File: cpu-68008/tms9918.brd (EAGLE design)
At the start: 99.7 x 99.7 mm, 38 parts, among them IC1 74HCT574N, IC101 GAL22V10D, IC2 74HCT574N, IC3 74HCT574N, IC4 74HCT04N, IC5 AS6C62256, IC6 74HCT373N, IC7 TMS9918, Q401 10.73866 MHz, T1 2N3904

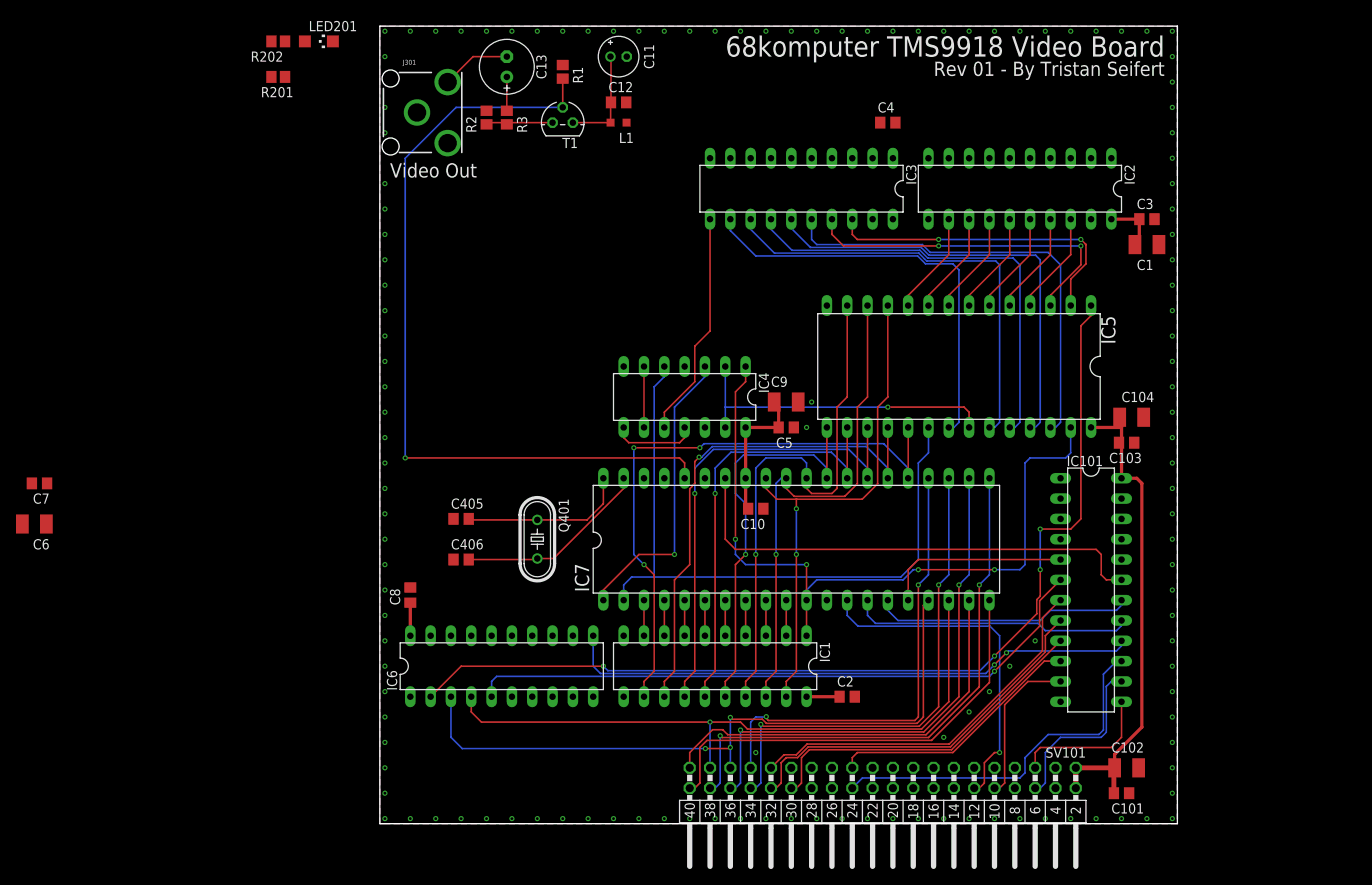
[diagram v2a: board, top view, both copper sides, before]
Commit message: minor revisions on mouser parts
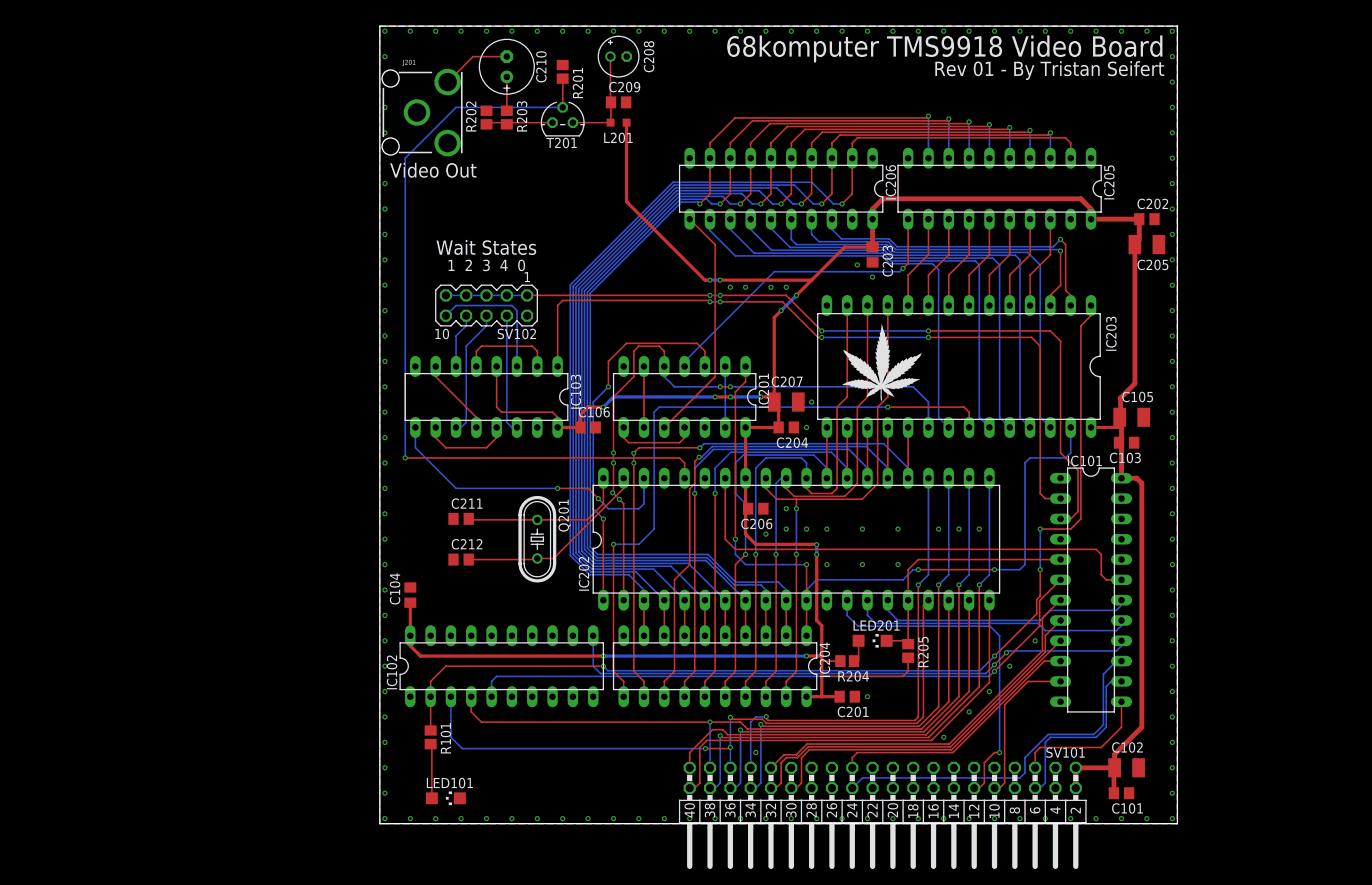
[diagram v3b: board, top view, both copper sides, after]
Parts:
- removed C4, C7, C8: 100nF, rcl:C0805
- removed C6: 10µF, rcl:SMC_B
- removed IC2, IC3: 74HCT574N, 74xx-eu:DIL20
- removed R1: 470R, rcl:R2012
- removed R2: 75R, rcl:R2012
- added C105: 10µF, rcl:SMC_B
- added C106, C203: 100nF, rcl:C0805
- added IC103: 74HCT175N, 74xx-eu:DIL16
- added IC205, IC206: 74HCT574N, 74xx-eu:DIL20
- added LED101: (no value), led:CHIPLED_1206
- added R101, R204: 3k, rcl:R2012
- added R205: 10k, rcl:R2012
- added SV102: (no value), con-lstb:MA05-2
- added WEED1: WEED, 68komputer:DOINK
- C104: value 10µF -> 100nF; device rcl:SMC_B -> rcl:C0805
- R201: value 10k -> 470R
- R202: value 3k -> 75R
- moved LED201 102.0 mm to (61.6, 22.9)
- moved C104 92.9 mm to (3.81, 28.6), turned to 90 degrees
- moved R201 35.6 mm to (22.9, 94.0), turned to 270 degrees
- moved R202 27.7 mm to (13.3, 88.3), turned to 270 degrees
- renumbered C1 to C205, C10 to C206, C11 to C208, C12 to C209, C13 to C210, C2 to C201, C3 to C202, C405 to C211, C406 to C212, C5 to C204, C9 to C207, IC1 to IC204, IC4 to IC201, IC5 to IC203, IC6 to IC102, IC7 to IC202, J301 to J201, L1 to L201, Q401 to Q201, R3 to R203, T1 to T201
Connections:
- removed net !ATA_ACTY: LED201.C
- new net !ACCESS_TIMER_CLEAR: IC101.2, IC103.1
- new net !DONE_1: IC103.3, SV102.10
- new net !DONE_2: IC103.6, SV102.8
- new net !DONE_3: IC103.11, SV102.6
- new net !DONE_4: IC103.14, SV102.4
- new net !TMS_DONE: IC101.3, SV102.1, SV102.3, SV102.5, SV102.7, SV102.9
- new net N$10: IC103.10, IC103.13
- new net N$11: LED101.A, R101.2
- new net N$8: IC103.2, IC103.5
- new net N$9: IC103.12, IC103.7
- new net TMS_CLK24: IC202.37
- new net TMS_CLK3: IC103.9, IC202.38
- net !TMS_IRQ: now also LED201.C, R205.1; no longer R201.1
- net +5V: now also C104.1, C105.+, C106.1, C203.1, IC103.16, IC103.4, IC205.20, IC206.20, R204.1, R205.2; no longer C104.+, C4.1, C6.+, C7.1, C8.1, IC2.20, IC3.20, R201.2, R202.1
- net COL: now also IC206.11; no longer IC3.11
- net GND: now also C104.2, C105.-, C106.2, C203.2, IC103.8, IC205.1, IC205.10, IC206.1, IC206.10, LED101.C, R201.1, R202.1, SV102.2; no longer C104.-, C4.2, C6.-, C7.2, C8.2, IC2.1, IC2.10, IC3.1, IC3.10, R1.1, R2.1
- net N$4: now also R202.2; no longer R2.2
- net N$7: now also R204.2; no longer R202.2
- net ROW: now also IC205.11; no longer IC2.11
- net TMS_AD0: now also IC205.9, IC206.9; no longer IC2.9, IC3.9
- net TMS_AD1: now also IC205.8, IC206.8; no longer IC2.8, IC3.8
- net TMS_AD2: now also IC205.7, IC206.7; no longer IC2.7, IC3.7
- net TMS_AD3: now also IC205.6, IC206.6; no longer IC2.6, IC3.6
- net TMS_AD4: now also IC205.5, IC206.5; no longer IC2.5, IC3.5
- net TMS_AD5: now also IC205.4, IC206.4; no longer IC2.4, IC3.4
- net TMS_AD6: now also IC205.3, IC206.3; no longer IC2.3, IC3.3
- net TMS_AD7: now also IC205.2, IC206.2; no longer IC2.2, IC3.2
- net TMS_VID_OUT: now also R201.2; no longer R1.2
- net VRAM_A0: now also IC205.12; no longer IC2.12
- net VRAM_A1: now also IC205.13; no longer IC2.13
- net VRAM_A10: now also IC206.12; no longer IC3.12
- net VRAM_A11: now also IC206.13; no longer IC3.13
- net VRAM_A12: now also IC206.18; no longer IC3.18
- net VRAM_A13: now also IC206.16; no longer IC3.16
- net VRAM_A2: now also IC205.14; no longer IC2.14
- net VRAM_A3: now also IC205.15; no longer IC2.15
- net VRAM_A4: now also IC205.16; no longer IC2.16
- net VRAM_A5: now also IC205.17; no longer IC2.17
- net VRAM_A6: now also IC205.18; no longer IC2.18
- net VRAM_A7: now also IC206.17; no longer IC3.17
- net VRAM_A8: now also IC206.15; no longer IC3.15
- net VRAM_A9: now also IC206.14; no longer IC3.14
- net VRAM_BANK: now also R101.1
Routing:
- net +5V: track 95.1 -> 362.9 mm, vias 0 -> 12
- net TMS_AD7: track 4.45 -> 128.8 mm, vias 0 -> 1
- net TMS_AD6: track 4.45 -> 128.2 mm, vias 0 -> 2
- net TMS_AD5: track 4.45 -> 127.4 mm, vias 0 -> 2
- net TMS_AD4: track 4.45 -> 126.7 mm, vias 0 -> 2
- net TMS_AD3: track 4.45 -> 126.1 mm, vias 0 -> 2
- net TMS_AD1: track 4.45 -> 125.4 mm, vias 0 -> 2
- net TMS_AD2: track 4.45 -> 125.4 mm, vias 0 -> 2
- net TMS_AD0: track 4.45 -> 124.8 mm, vias 0 -> 2
- net !TMS_DONE: track 0.00 -> 104.0 mm, vias 0 -> 4
- net !ACCESS_TIMER_CLEAR: track 0.00 -> 91.8 mm, vias 0 -> 4
- net !TMS_RD: track 40.3 -> 89.5 mm, vias 1 -> 2
- net ROW: track 0.00 -> 39.2 mm, vias 0 -> 1
- net TMS_CLK3: track 0.00 -> 37.7 mm, vias 0 -> 2
- net !DONE_1: track 0.00 -> 16.7 mm
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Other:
- board text added: "1 2 3 4 0"
- board text added: "Wait States"
